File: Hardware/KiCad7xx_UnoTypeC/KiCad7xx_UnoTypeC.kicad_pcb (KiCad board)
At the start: 2 copper layers, 68.6 x 53.3 mm, 119 parts, among them T1 FDN340P, U1 NCP1117ST50T3G, U2 LP2985-33DBVR, U3 ATMEGA16U2-MU(R), U5 LMV358IDGKR, X1 POWERSUPPLY_DC21MMX, X2 USB-B_TH, Y1 16MHz, Y2 CSTCE16M0V53-R0 16MHZ

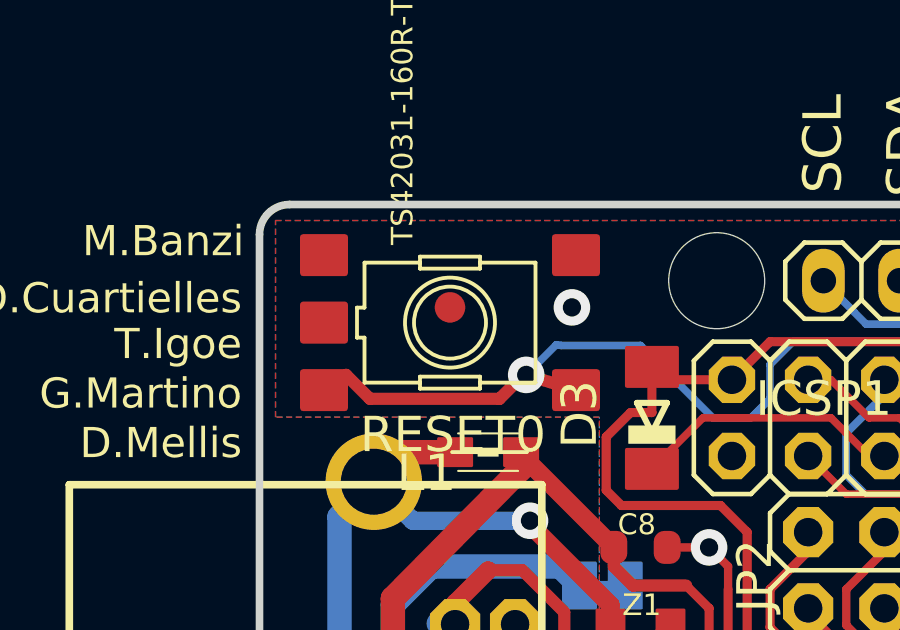
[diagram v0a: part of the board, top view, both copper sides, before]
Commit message: feat: KiCad7xx_UnoTypeCにて既存のUnoRev3回路図をType-Cに変更
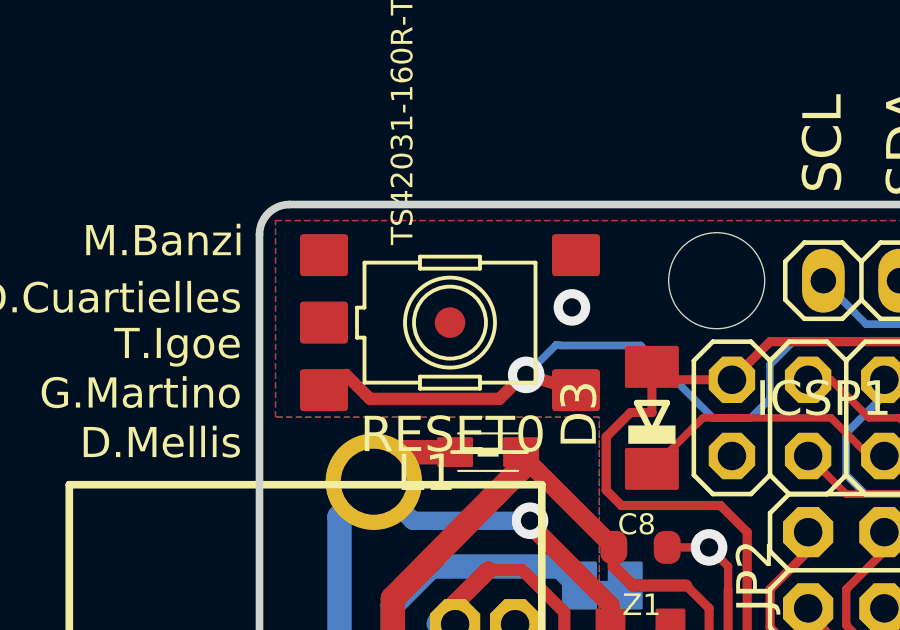
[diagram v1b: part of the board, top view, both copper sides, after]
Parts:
- moved FD1 0.51 mm to (120.6, 82.3)
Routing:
- net UGND: track 39.6 -> 0.00 mm
- net GND: track 14.2 -> 53.8 mm

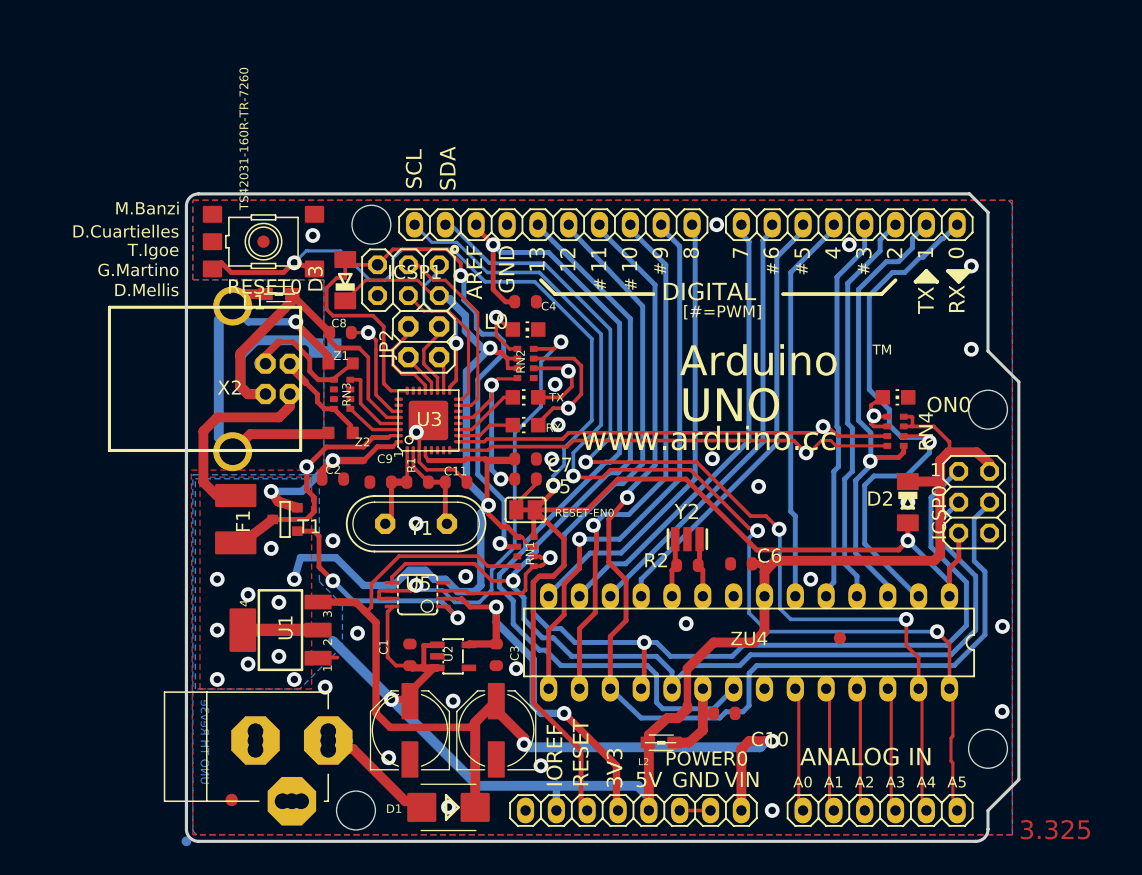
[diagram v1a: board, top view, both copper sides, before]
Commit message: feat: PCBにTypeCの配線を追加
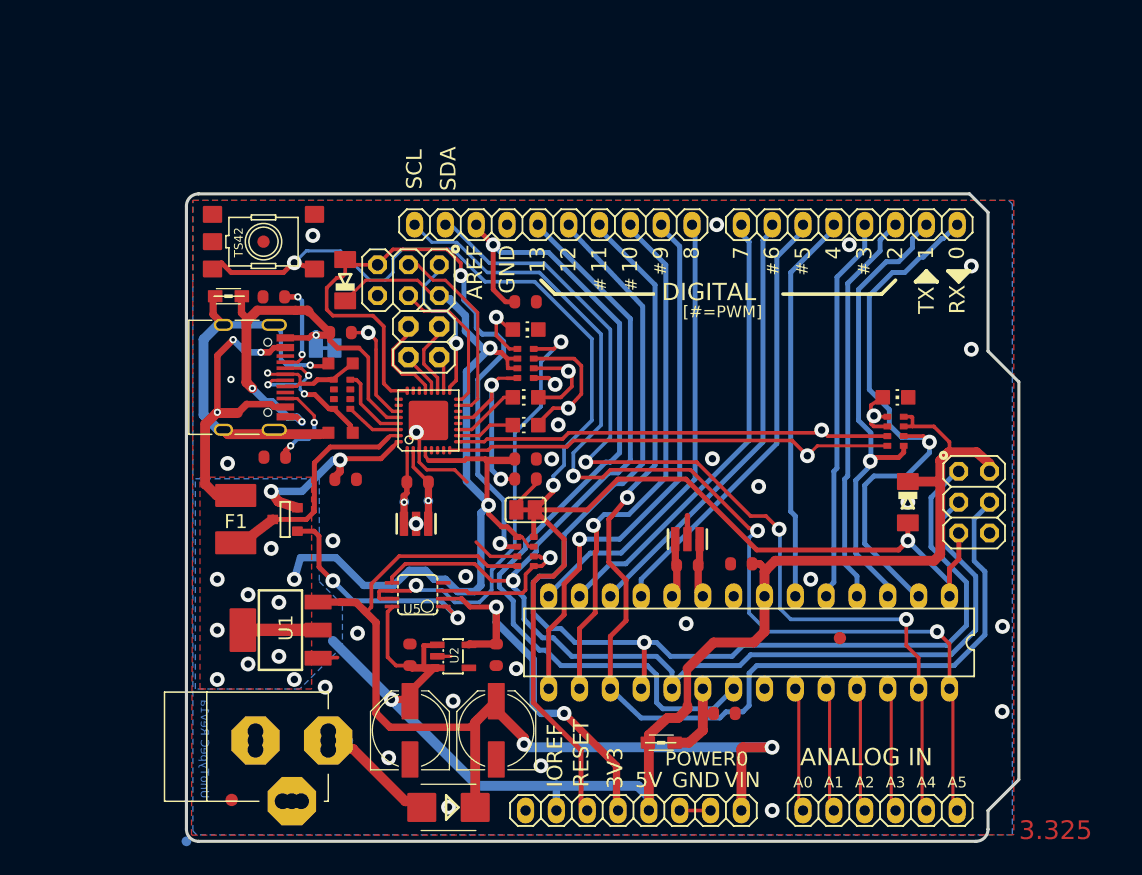
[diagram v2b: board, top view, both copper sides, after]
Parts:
- removed @HOLE0, @HOLE1, @HOLE2, @HOLE3: , 
- removed C11, C9: 22p, UNO-TH_Rev3e:C0603-ROUND
- removed TP_D+0, TP_D-0, TP_UGND0, TP_USBVCC0, TP_USH0, TP_XUSB0: TP_SP, UNO-TH_Rev3e:TP-SP
- removed X2: USB-B_TH, UNO-TH_Rev3e:PN61729
- added J1: USB_C_Receptacle_USB2.0, Connector_USB:USB_C_Receptacle_HRO_TYPE-C-31-M-12, F.Cu at (118.3, 93.4)
- added R3: 5.1k, UNO-TH_Rev3e:R0603-ROUND, F.Cu at (121.4, 86.8)
- added R4: 5.1k, UNO-TH_Rev3e:R0603-ROUND, F.Cu at (121.5, 100.0)
- GROUND0, RESET-EN0: value (none) -> SJ
- RESET0: value TS42031-160R-TR-7260 -> TS42
- U1: value NCP1117ST50T3G -> MC33269ST
- U2: value LP2985-33DBVR -> LP2985-XXDBVR
- U3: value ATMEGA16U2-MU(R) -> ATMEGA16U2-MU
- U5: value LMV358IDGKR -> LMV358?MM
- Y1: value 16MHz -> RESONATORMU; footprint UNO-TH_Rev3e:QS -> UNO-TH_Rev3e:RESONATOR
- Y2: value CSTCE16M0V53-R0 16MHZ -> RESONATORMU
- Z1, Z2: value CG0603MLC-05E -> VARISTORCN0603
- moved L1 4.16 mm to (117.7, 86.8)
- moved TP_XT4 2.43 mm to (134.1, 103.6)
- moved TP_XT3 2.39 mm to (132.2, 103.7)
- moved C2 1.05 mm to (127.3, 101.9)
- moved TP_RX0 0.30 mm to (166.5, 97.8)
- moved TP_TX0 0.26 mm to (165.4, 99.9)
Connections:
- net +3V3 renamed /+3V3
- net AD0 renamed /AD0
- net AD1 renamed /AD1
- net AD2 renamed /AD2
- net AD3 renamed /AD3
- net AD4/SDA renamed /AD4/SDA
- net AD5/SCL renamed /AD5/SCL
- net AREF renamed /AREF
- net AVCC renamed /AVCC
- net CMP renamed /CMP
- net D+ renamed /D+
- net D- renamed /D-
- net DTR renamed /DTR
- net GATE_CMD renamed /GATE_CMD
- net IO0 renamed /IO0
- net IO1 renamed /IO1
- net IO2 renamed /IO2
- net IO3 renamed /IO3
- net IO4 renamed /IO4
- net IO5 renamed /IO5
- net IO6 renamed /IO6
- net IO7 renamed /IO7
- net IO8 renamed /IO8
- net IO9 renamed /IO9
- net L13 renamed /L13
- net M8RXD renamed /M8RXD
- net M8TXD renamed /M8TXD
- net MISO renamed /MISO
- net MISO2 renamed /MISO2
- net MOSI renamed /MOSI
- net MOSI2 renamed /MOSI2
- net PB4 renamed /PB4
- net PB5 renamed /PB5
- net PB6 renamed /PB6
- net PB7 renamed /PB7
- net PWRIN renamed /PWRIN
- net RD+ renamed /RD+
- net RD- renamed /RD-
- net RESET renamed /RESET
- net RESET2 renamed /RESET2
- net RXLED renamed /RXLED
- net SCK renamed /SCK
- net SCK2 renamed /SCK2
- net SS renamed /SS
- net TP_VUCAP renamed /TP_VUCAP
- net TXLED renamed /TXLED
- net USBVCC renamed /USBVCC
- net USHIELD renamed /USHIELD
- net VIN renamed /VIN
- net XT2 renamed /XT2
- net XTAL1 renamed /XTAL1
- net XTAL2 renamed /XTAL2
- C8 pad 2: UGND -> /UGND
- F1 pad 2: XUSB -> /XUSB
- GROUND0 pad 1: GND -> /UGND
- GROUND0 pad 2: UGND -> /UGND
- L1 pad 1: UGND -> /UGND
- ORIGIN0 pad X: (no net) -> unconnected-(ORIGIN0-TESTP-PadX)
- POWER0 pad 1: (no net) -> unconnected-(POWER0-Pad1)
- R1 pad 1: XT1 -> /XT1
- RN3 pad 2: (no net) -> unconnected-(RN3B-1-Pad2)
- RN3 pad 3: (no net) -> unconnected-(RN3C-1-Pad3)
- RN3 pad 6: (no net) -> unconnected-(RN3C-2-Pad6)
- RN3 pad 7: (no net) -> unconnected-(RN3B-2-Pad7)
- TP_XT3 pad X: XT1 -> /XT1
- U2 pad 4: (no net) -> unconnected-(U2-NC/FB-Pad4)
- U3 pad 1: XT1 -> /XT1
- U3 pad 12: (no net) -> unconnected-(U3-(RTS/AIN5/INT6)PD6-Pad12)
- U3 pad 14: (no net) -> unconnected-(U3-(SS/PCINT0)PB0-Pad14)
- U3 pad 22: (no net) -> unconnected-(U3-(INT4/ICP1/CLK0)PC7-Pad22)
- U3 pad 23: (no net) -> unconnected-(U3-(OC1A/PCINT8)PC6-Pad23)
- U3 pad 25: (no net) -> unconnected-(U3-(PCINT9/OC1B)PC5-Pad25)
- U3 pad 26: (no net) -> unconnected-(U3-(PCINT10)PC4-Pad26)
- U3 pad 28: UGND -> /UGND
- U3 pad 5: (no net) -> unconnected-(U3-(AIN2/PCINT11)PC2-Pad5)
- U3 pad 6: (no net) -> unconnected-(U3-(OC0B/INT0)PD0-Pad6)
- U3 pad 7: (no net) -> unconnected-(U3-(AIN0/INT1)PD1-Pad7)
- Y1 pad 2: XT1 -> GND
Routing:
- net /UGND: track 0.00 -> 39.7 mm, vias 0 -> 3
- net GND: track 53.8 -> 21.7 mm, vias 27 -> 29
- net /XUSB: track 0.00 -> 29.9 mm, vias 0 -> 3
- net XUSB: track 16.3 -> 0.00 mm
- net Net-(J1-CC2): track 0.00 -> 8.09 mm, vias 0 -> 2
- net XT1: track 7.91 -> 0.00 mm
- net Net-(J1-CC1): track 0.00 -> 7.79 mm, vias 0 -> 2
- net /XT1: track 0.00 -> 6.37 mm, vias 0 -> 1
- net /D-: track 8.27 -> 13.9 mm, vias 0 -> 3
- net /D+: track 11.4 -> 9.75 mm, vias 0 -> 1
- net /XT2: track 8.03 -> 6.59 mm, vias 0 -> 1
- net /USHIELD: track 34.9 -> 34.0 mm
- net /USBVCC: track 21.2 -> 20.5 mm, vias 1 -> 0
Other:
- board text added: "UnoTypeC Rev1a"
- board text removed: "Arduino"
- board text removed: "D.Cuartielles"
- board text removed: "D.Mellis"
- board text removed: "G.Martino"
- board text removed: "ITALY"
- board text removed: "M.Banzi"
- board text removed: "MADE IN"
- board text removed: "T.Igoe"
- board text removed: "TM"
- board text removed: "UNO"
- board text removed: "UNO TH Rev3e"
- board text removed: "designed by"
- board text removed: "tinker it"
- board text removed: "www.arduino.cc"

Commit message: feat: Gerberとシルクデザインの作成
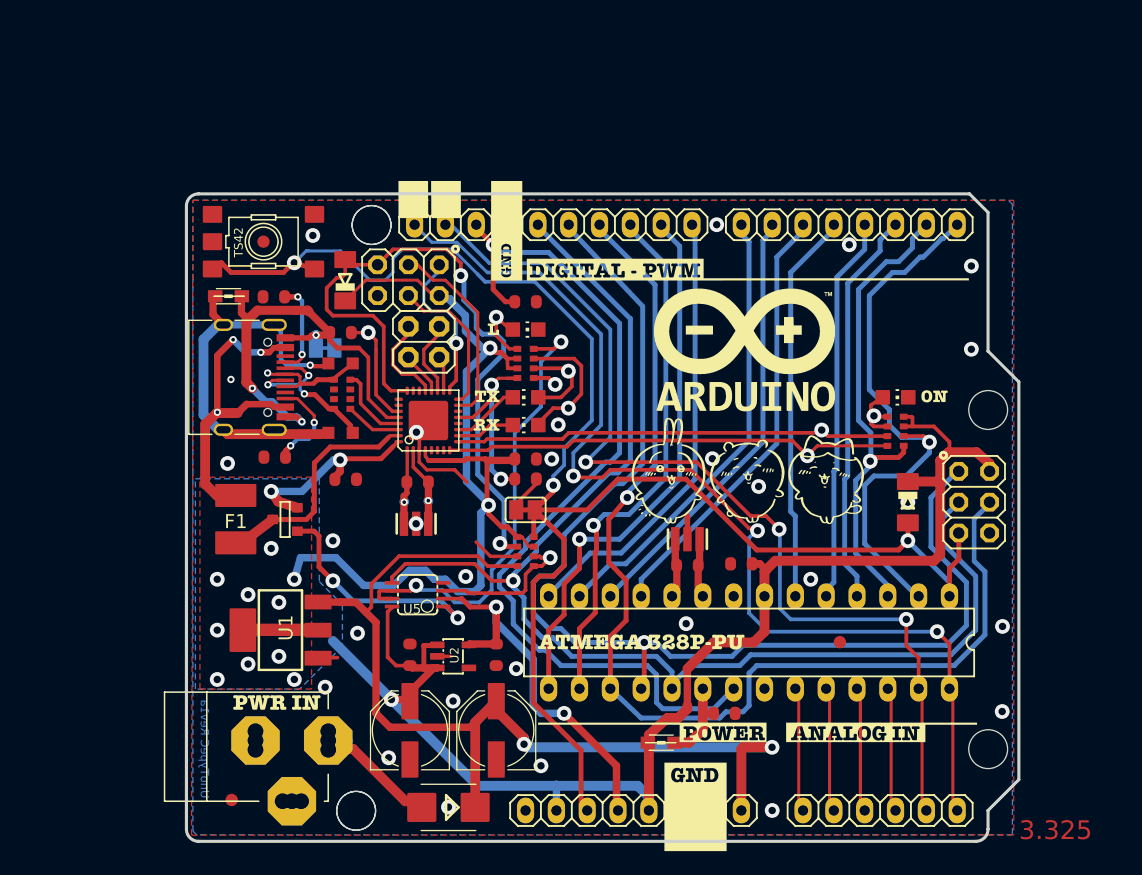
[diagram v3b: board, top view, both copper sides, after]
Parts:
- removed ORIGIN0: TP_SP, UNO-TH_Rev3e:TP-SP
- added ?, @HOLE2: , , F.Cu at (129.5, 80.9)
- added ?, @HOLE3: , , F.Cu at (128.2, 129.2)
- added @HOLE0: , , F.Cu at (180.3, 96.1)
- added @HOLE1: , , F.Cu at (180.3, 124.1)
- added G***: LOGO, footprint:シルク_Front_Rev1b_55-2, F.Cu at (148.7, 104.9)
- added G***: LOGO, footprint:シルク_Back_Rev1a_58, B.Cu at (148.3, 105.5)
- moved FD2 0.33 mm to (168.0, 115.3)
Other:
- board text removed: "#"
- board text removed: "0"
- board text removed: "1"
- board text removed: "10"
- board text removed: "11"
- board text removed: "12"
- board text removed: "13"
- board text removed: "2"
- board text removed: "3"
- board text removed: "3V3"
- board text removed: "4"
- board text removed: "5"
- board text removed: "5V"
- board text removed: "6"
- board text removed: "7"
- board text removed: "8"
- board text removed: "9"
- board text removed: "A0"
- board text removed: "A1"
- board text removed: "A2"
- board text removed: "A3"
- board text removed: "A4"
- board text removed: "A5"
- board text removed: "ANALOG IN"
- board text removed: "AREF"
- board text removed: "DIGITAL"
- board text removed: "GND"
- board text removed: "IOREF"
- board text removed: "RESET"
- board text removed: "SCL"
- board text removed: "SDA"
- board text removed: "VIN"
- board text removed: "[#=PWM]"
